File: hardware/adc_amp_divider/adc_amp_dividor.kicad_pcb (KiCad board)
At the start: 2 copper layers, 94 parts, among them M1 CONN_1, M2 CONN_1, P1 CONN_10X2, P2 CONN_4, P3 CONN_6, P4 CONN_3, U1 LMV324IDR, U2 LMV324IDR, U3 LMV324IDR

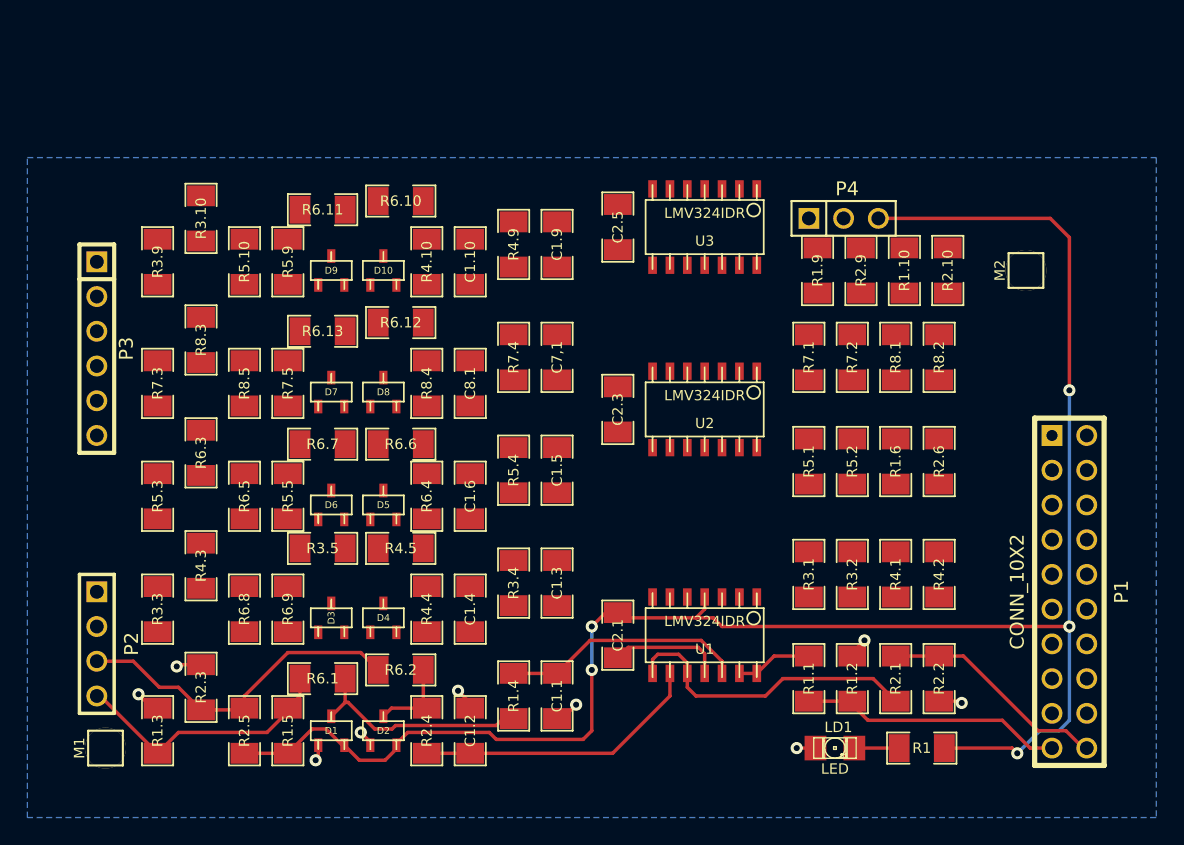
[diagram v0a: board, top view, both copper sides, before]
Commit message: 
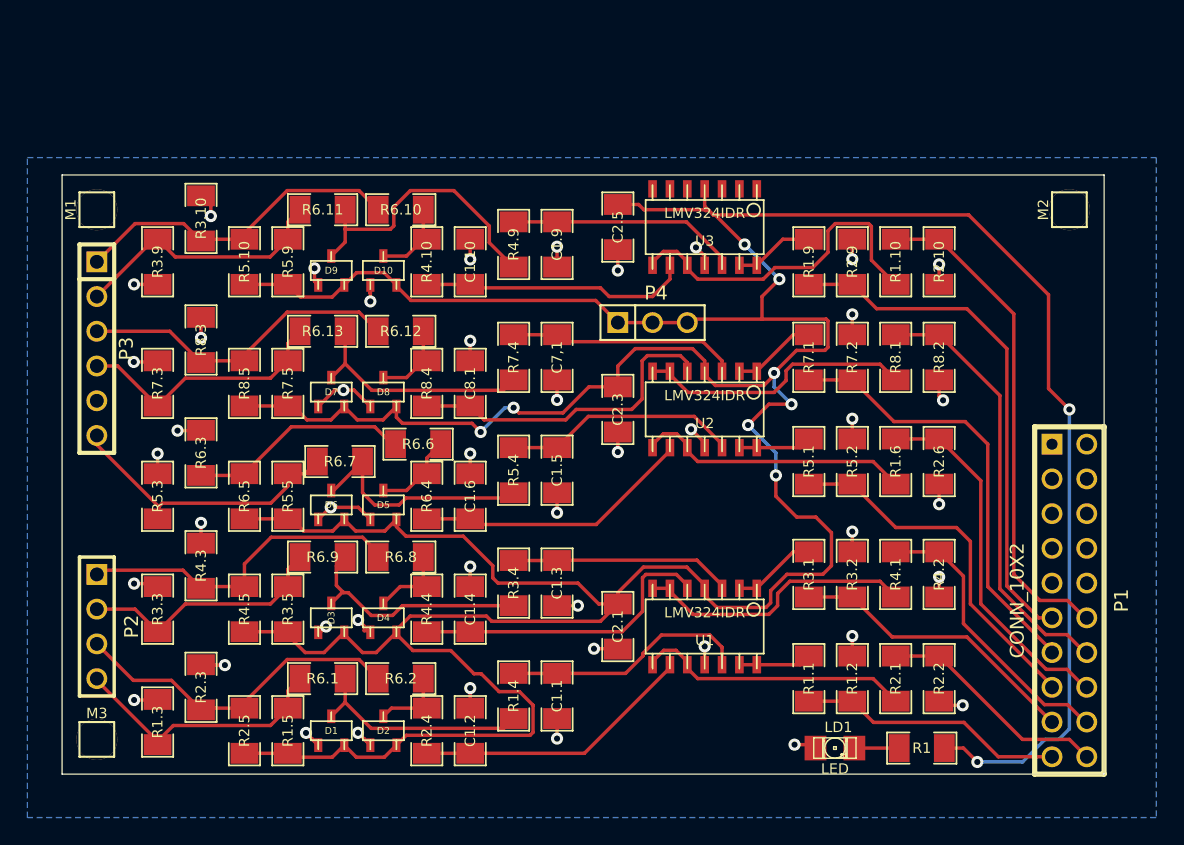
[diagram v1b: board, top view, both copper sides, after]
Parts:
- added M3: CONN_1, PIN_ARRAY_1, F.Cu at (92.7, 169.5)
- moved M1 39.4 mm to (92.7, 130.8)
- moved P4 15.9 mm to (133.3, 139.1)
- moved R4.5 12.3 mm to (103.5, 160.0), turned to 270 degrees
- moved R6.8 12.0 mm to (114.9, 156.2), turned to 0 degrees
- moved M2 5.46 mm to (163.8, 130.8)
- moved R3.5 5.12 mm to (106.7, 160.0), turned to 270 degrees
- moved R6.9 4.58 mm to (109.2, 156.2), turned to 0 degrees
- moved R6.7 1.80 mm to (110.5, 149.2)
- moved P2 1.27 mm to (92.7, 161.3)
- moved R6.6 1.27 mm to (116.2, 148.0)
- moved R1.10 0.90 mm to (151.1, 134.6)
- moved R1.9 0.90 mm to (144.8, 134.6)
- moved R2.10 0.90 mm to (154.3, 134.6)
- moved R2.9 0.90 mm to (148.0, 134.6)
- moved C2.1 0.64 mm to (130.8, 161.3)
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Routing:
- net VCC: track 134.0 -> 330.3 mm, vias 5 -> 10
- net GND: track 22.6 -> 76.8 mm, vias 9 -> 45
- net /OUT9: track 0.00 -> 38.0 mm
- net /OUT10: track 0.00 -> 36.6 mm
- net /OUT7: track 0.00 -> 32.2 mm
- net /OUT8: track 0.00 -> 31.9 mm
- net /OUT6: track 0.00 -> 26.8 mm
- net /OUT5: track 0.00 -> 26.7 mm
- net N-0000052: track 0.00 -> 25.4 mm
- net /INP10: track 0.00 -> 24.6 mm
- net /INP4: track 0.00 -> 24.5 mm
- net N-0000011: track 0.00 -> 23.9 mm
- net /INP8: track 0.00 -> 23.9 mm
- net N-0000065: track 0.00 -> 22.8 mm
- net /OUT3: track 0.00 -> 21.6 mm
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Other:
- board outline added: 76.2 x 43.8 mm
- net class Default: clearance 0.254 -> 0.2032
- rule trace_clearance: 0.254 -> 0.2032

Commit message: now 12 channels
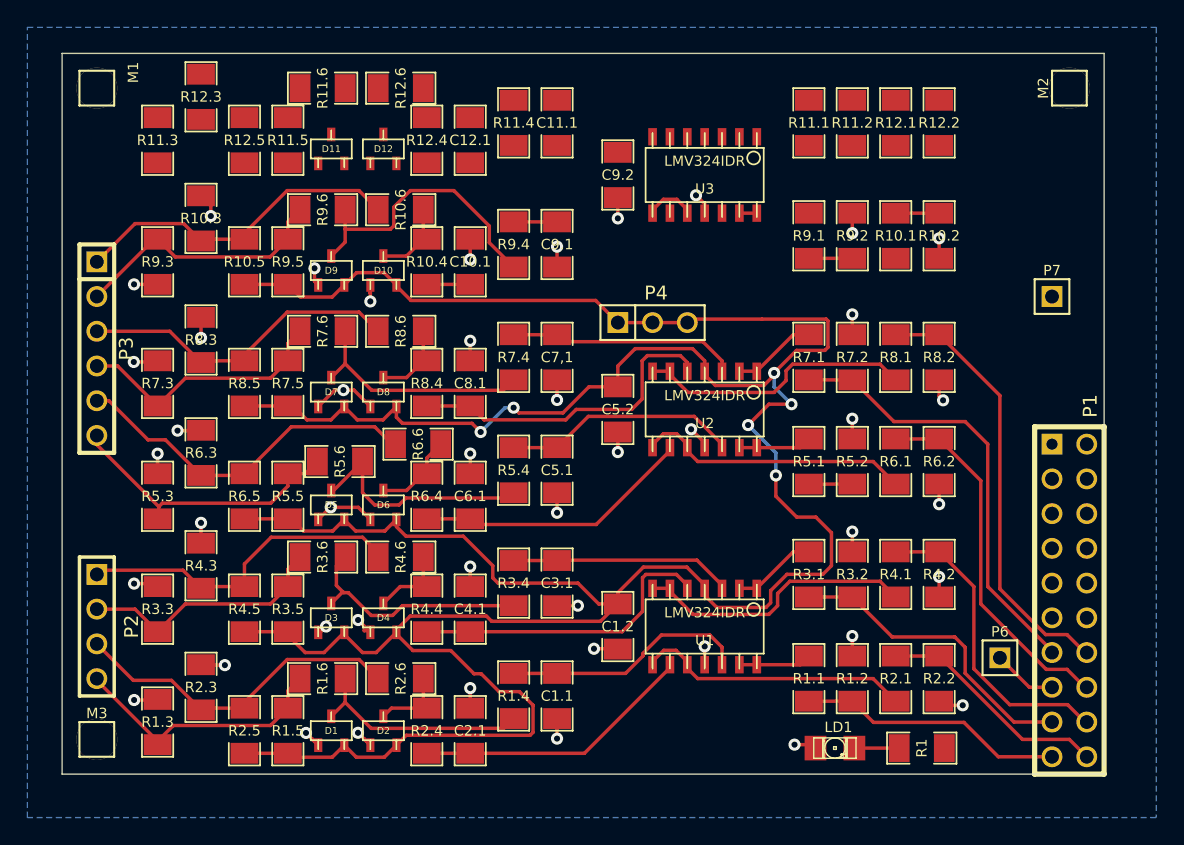
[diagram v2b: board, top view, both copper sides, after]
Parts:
- added C11.1: 0.01uF, SM1206, F.Cu at (126.4, 124.5)
- added C12.1: 0.01uF, SM1206, F.Cu at (120.0, 125.7)
- added D11: DOUBLE_SCHOTTKY, sot23, F.Cu at (109.9, 126.4)
- added D12: DOUBLE_SCHOTTKY, sot23, F.Cu at (113.7, 126.4)
- added P6: CONN_1, PIN_ARRAY_1, F.Cu at (158.8, 163.6)
- added P7: CONN_1, PIN_ARRAY_1, F.Cu at (162.6, 137.2)
- added R11.1: 1500, SM1206, F.Cu at (144.8, 124.5)
- added R11.2: 1500, SM1206, F.Cu at (148.0, 124.5)
- added R11.3: 500K, SM1206, F.Cu at (97.2, 125.7)
- added R11.4: 150, SM1206, F.Cu at (123.2, 124.5)
- added R11.5: 2700, SM1206, F.Cu at (106.7, 125.7)
- added R11.6: 10k, SM1206, F.Cu at (109.2, 121.9)
- added R12.1: 1500, SM1206, F.Cu at (151.1, 124.5)
- added R12.2: 1500, SM1206, F.Cu at (154.3, 124.5)
- added R12.3: 500K, SM1206, F.Cu at (100.3, 122.6)
- added R12.4: 150, SM1206, F.Cu at (116.8, 125.7)
- added R12.5: 2700, SM1206, F.Cu at (103.5, 125.7)
- added R12.6: 10k, SM1206, F.Cu at (114.9, 121.9)
- moved M1 8.89 mm to (92.7, 121.9)
- moved M2 8.89 mm to (163.8, 121.9)
- moved C9.2 3.81 mm to (130.8, 128.3)
- moved U3 3.81 mm to (137.2, 128.3)
- moved R10.1 1.91 mm to (151.1, 132.7)
- moved R10.2 1.91 mm to (154.3, 132.7)
- moved R9.1 1.91 mm to (144.8, 132.7)
- moved R9.2 1.91 mm to (148.0, 132.7)
- renumbered C2.1 to C1.2, C1.10 to C10.1, C1.2 to C2.1, C1.3 to C3.1, C1.4 to C4.1, C1.5 to C5.1, C2.3 to C5.2, C1.6 to C6.1, C1.9 to C9.1, C2.5 to C9.2, D6 to D5, D5 to D6, R6.1 to R1.6, R1.10 to R10.1, R2.10 to R10.2, R3.10 to R10.3, R4.10 to R10.4, R5.10 to R10.5, R6.10 to R10.6, R6.2 to R2.6, R6.9 to R3.6, R6.8 to R4.6, R6.7 to R5.6, R1.6 to R6.1, R2.6 to R6.2, R6.13 to R7.6, R6.12 to R8.6, R1.9 to R9.1, R2.9 to R9.2, R3.9 to R9.3, R4.9 to R9.4, R5.9 to R9.5, R6.11 to R9.6
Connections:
- P1 pad 10: (no net) -> /OUT11
- P1 pad 11: /OUT9 -> /OUT8
- P1 pad 12: /OUT10 -> /OUT9
- P1 pad 13: /OUT7 -> /OUT6
- P1 pad 14: /OUT8 -> /OUT7
- P1 pad 15: /OUT5 -> /PA5
- P1 pad 16: /OUT6 -> /OUT5
- P1 pad 7: (no net) -> /OUT12
- P1 pad 8: (no net) -> /PC0
- P1 pad 9: (no net) -> /OUT10
- P3 pad 5: (no net) -> /INP6
- R6.3 pad 1: N-0000079 (its old number) -> /INP6
- R6.5 pad 1: N-0000079 (its old number) -> /INP6
- R6.6 pad 1: N-0000079 (its old number) -> /INP6
- U3 pad 1: (no net) -> N-0000026
- U3 pad 2: (no net) -> N-0000026
- U3 pad 3: (no net) -> N-0000032
- U3 pad 5: (no net) -> N-0000035
- U3 pad 6: (no net) -> N-0000027
- U3 pad 7: (no net) -> N-0000027
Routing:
- net VCC: track 330.3 -> 241.2 mm, vias 10 -> 6
- net /OUT9: track 38.0 -> 3.18 mm
- net /OUT10: track 36.6 -> 3.18 mm
- net /INP6: track 0.00 -> 26.1 mm
- net /OUT8: track 31.9 -> 9.46 mm
- net N-0000012: track 25.4 -> 3.66 mm
- net N-000004: track 19.7 -> 3.17 mm
- net N-0000079 (its old number): track 16.2 -> 0.00 mm
- net N-000003: track 16.9 -> 3.17 mm
- net /OUT6: track 26.8 -> 32.2 mm
- net /PA5: track 0.00 -> 4.70 mm
- net N-0000011: track 5.87 -> 1.27 mm
- net /OUT5: track 26.7 -> 22.5 mm
- net /OUT7: track 32.2 -> 29.9 mm
- net /OUT4: track 21.2 -> 22.6 mm
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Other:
- board size 76.2 x 43.8 mm -> 76.2 x 52.7 mm

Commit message: my changes
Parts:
- added P8: CONN_2, PIN_ARRAY_2X1, F.Cu at (132.1, 121.9)
- P4: value CONN_3 -> CONN_2; footprint PIN_ARRAY_3X1 -> PIN_ARRAY_2X1
- moved P7 40.2 mm to (139.7, 170.2)
- moved P6 25.0 mm to (134.6, 170.2)
- moved P4 19.3 mm to (142.2, 121.9)
- moved C9.2 4.58 mm to (133.3, 132.1)
- moved U3 4.58 mm to (139.7, 132.1)
- moved R10.1 3.81 mm to (154.9, 132.7)
- moved R10.2 3.81 mm to (158.1, 132.7)
- moved R11.1 3.81 mm to (148.6, 124.5)
- moved R12.1 3.81 mm to (154.9, 124.5)
- moved R12.2 3.81 mm to (158.1, 124.5)
- moved R9.1 3.81 mm to (148.6, 132.7)
- moved R11.2 3.81 mm to (151.8, 124.5)
- moved R9.2 3.81 mm to (151.8, 132.7)
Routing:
- net /OUT6: track 32.2 -> 3.18 mm
- net VCC: track 241.2 -> 269.9 mm
- net /OUT7: track 29.9 -> 3.18 mm
- net /PA5: track 4.70 -> 28.3 mm
- net /OUT5: track 22.5 -> 3.18 mm
- net GND: track 76.8 -> 83.1 mm
- net /OUT8: track 9.46 -> 3.18 mm
- net N-000009: track 3.66 -> 0.00 mm

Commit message: fresh version
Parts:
- removed P8: CONN_2, PIN_ARRAY_2X1
- added P5: CONN_2, SIL-2, F.Cu at (134.6, 134.0)
- P2: value CONN_4 -> CONN_6; footprint PIN_ARRAY_4x1 -> PIN_ARRAY-6X1
- P4: value CONN_2 -> CONN_3; footprint PIN_ARRAY_2X1 -> PIN_ARRAY_3X1
- moved P7 36.6 mm to (162.6, 141.6)
- moved LD1 35.3 mm to (141.6, 135.3), turned to 270 degrees
- moved R1 33.6 mm to (140.3, 139.1), turned to 0 degrees
- moved P6 25.0 mm to (158.8, 163.6)
- moved P4 18.8 mm to (133.3, 138.4)
- moved P3 7.01 mm to (92.1, 134.0)
- moved C9.2 5.12 mm to (130.8, 127.6)
- moved U3 5.12 mm to (137.2, 127.6)
- moved P2 5.12 mm to (92.1, 156.2)
- moved R10.1 3.86 mm to (151.1, 132.1)
- moved R10.2 3.86 mm to (154.3, 132.1)
- moved R11.1 3.86 mm to (144.8, 123.8)
- moved R12.1 3.86 mm to (151.1, 123.8)
- moved R12.2 3.86 mm to (154.3, 123.8)
- moved R9.1 3.86 mm to (144.8, 132.1)
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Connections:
- P1 pad 2: (no net) -> GND
- P2 pad 1: /INP4 -> /INP6
- P2 pad 2: /INP3 -> /INP5
- P2 pad 3: /INP2 -> /INP4
- P2 pad 4: /INP1 -> /INP3
- P3 pad 1: /INP10 -> /INP12
- P3 pad 2: /INP9 -> /INP11
- P3 pad 3: /INP8 -> /INP10
- P3 pad 4: /INP7 -> /INP9
- P3 pad 5: /INP6 -> /INP8
- P3 pad 6: /INP5 -> /INP7
- R11.3 pad 1: /INP9 -> /INP11
- R11.5 pad 1: /INP9 -> /INP11
- R11.6 pad 1: /INP9 -> /INP11
- R12.3 pad 1: /INP10 -> /INP12
- R12.5 pad 1: /INP10 -> /INP12
- R12.6 pad 1: /INP10 -> /INP12
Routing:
- net /OUT11: track 0.00 -> 51.3 mm
- net /OUT12: track 0.00 -> 42.1 mm
- net /OUT9: track 3.17 -> 41.1 mm
- net /OUT7: track 3.18 -> 38.9 mm
- net /OUT10: track 3.18 -> 35.7 mm
- net /INP12: track 0.00 -> 28.9 mm
- net /OUT8: track 3.18 -> 29.0 mm
- net /OUT5: track 3.18 -> 28.9 mm
- net N-0000026: track 0.00 -> 24.4 mm
- net /INP11: track 0.00 -> 24.2 mm
- net /PA5: track 28.3 -> 4.70 mm
- net N-0000024: track 0.00 -> 21.8 mm
- net N-0000010: track 0.00 -> 21.1 mm
- net /OUT6: track 3.18 -> 22.4 mm
- net N-0000025: track 0.00 -> 18.5 mm
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- added copper zone on F.Cu, net GND
- added copper zone on F.Cu, net VCC
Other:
- outline, holes or cut-outs redrawn

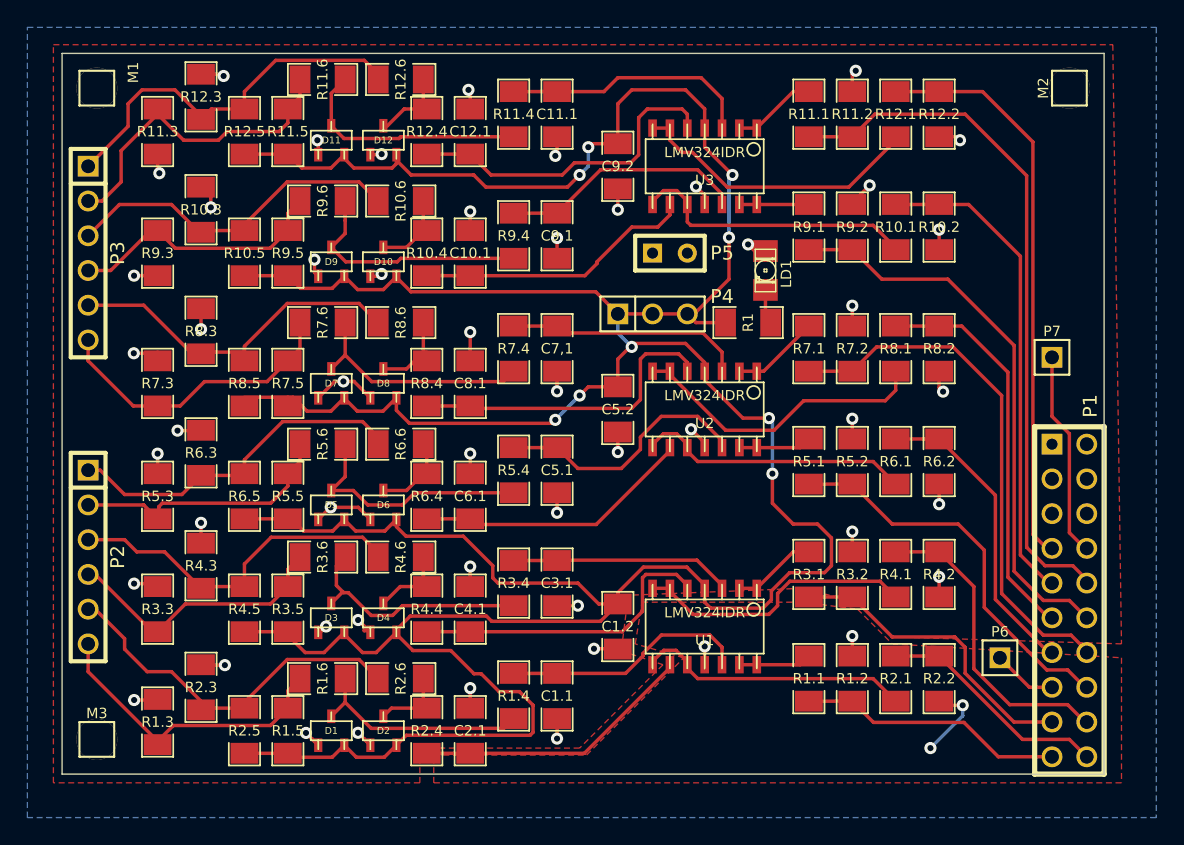
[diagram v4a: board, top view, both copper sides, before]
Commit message: 
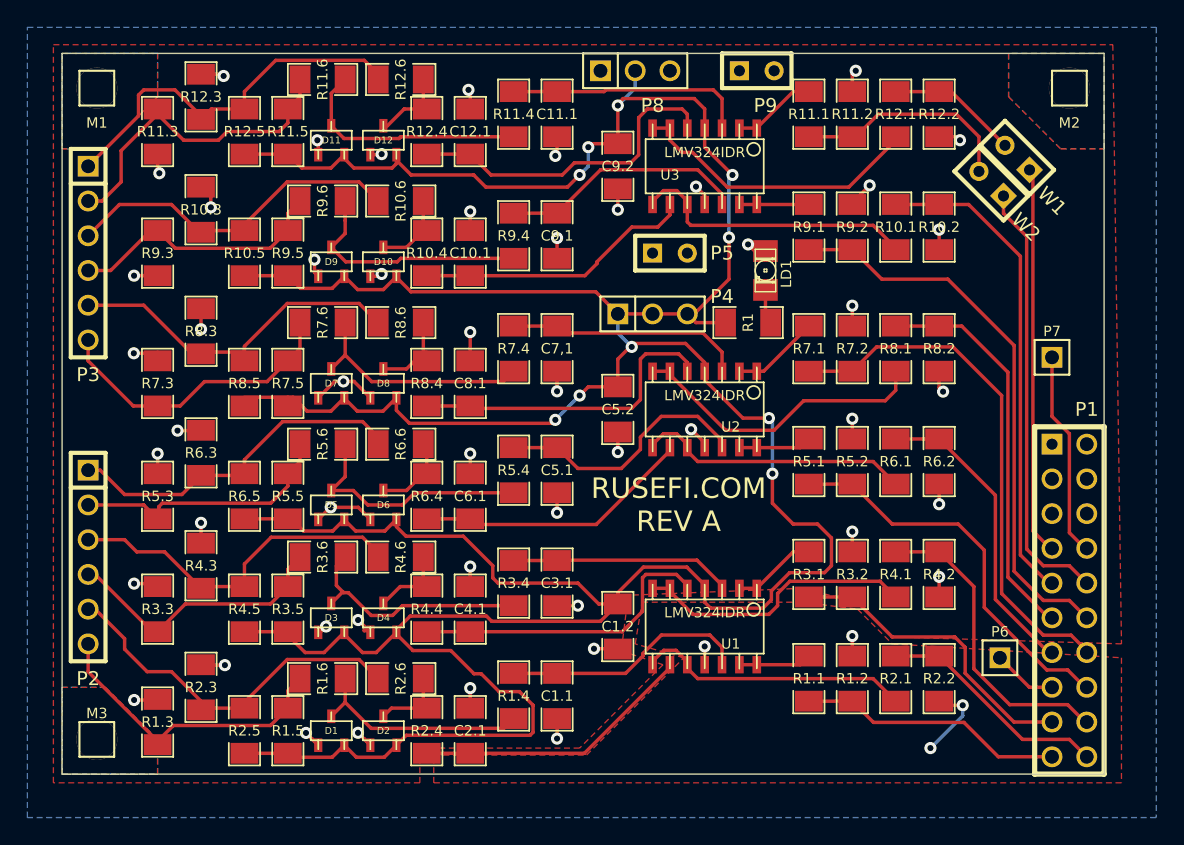
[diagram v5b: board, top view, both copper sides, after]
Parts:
- added P8: CONN_3, PIN_ARRAY_3X1, F.Cu at (132.1, 120.7)
- added P9: CONN_2, SIL-2, F.Cu at (141.0, 120.7)
- added W1: TEST, SIL-2, F.Cu at (160.0, 127.0)
- added W2: TEST, SIL-2, F.Cu at (158.1, 128.9)
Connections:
- R11.1 pad 2: /OUT11 -> N-0000035
- R11.2 pad 1: /OUT11 -> N-0000035
- R12.1 pad 2: /OUT12 -> N-0000034
- R12.2 pad 1: /OUT12 -> N-0000034
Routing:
- net /OUT11: track 51.3 -> 31.9 mm
- net N-0000035: track 0.00 -> 16.3 mm
- net /OUT12: track 42.1 -> 28.4 mm
- net N-0000034: track 0.00 -> 9.62 mm
- net VCC: track 284.8 -> 287.5 mm, vias 9 -> 10
- net N-0000030: track 18.5 -> 17.7 mm
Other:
- board text added: "RUSEFI.COM REV A"

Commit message: 150 > 100 on silkscreen
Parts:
- R1, R1.4, R10.4, R11.4, R12.4, R2.4, R3.4, R4.4, R5.4, R6.4, R7.4, R8.4, R9.4: value 150 -> 100
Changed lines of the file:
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@@
       (effects (font (size 0.762 0.762) (thickness 0.127)))
     )
-    (fp_text value 150 (at 0 0 90) (layer F.SilkS) hide
+    (fp_text value 100 (at 0 0 90) (layer F.SilkS) hide
       (effects (font (size 0.762 0.762) (thickness 0.127)))
     )
@@
       (effects (font (size 0.762 0.762) (thickness 0.127)))
     )
-    (fp_text value 150 (at 0 0 270) (layer F.SilkS) hide
+    (fp_text value 100 (at 0 0 270) (layer F.SilkS) hide
       (effects (font (size 0.762 0.762) (thickness 0.127)))
     )
@@
       (effects (font (size 0.762 0.762) (thickness 0.127)))
     )
-    (fp_text value 150 (at 0 0 90) (layer F.SilkS) hide
+    (fp_text value 100 (at 0 0 90) (layer F.SilkS) hide
       (effects (font (size 0.762 0.762) (thickness 0.127)))
     )
@@
       (effects (font (size 0.762 0.762) (thickness 0.127)))
     )
-    (fp_text value 150 (at 0 0 270) (layer F.SilkS) hide
+    (fp_text value 100 (at 0 0 270) (layer F.SilkS) hide
       (effects (font (size 0.762 0.762) (thickness 0.127)))
     )
@@
       (effects (font (size 0.762 0.762) (thickness 0.127)))
     )
-    (fp_text value 150 (at 0 0 270) (layer F.SilkS) hide
+    (fp_text value 100 (at 0 0 270) (layer F.SilkS) hide
       (effects (font (size 0.762 0.762) (thickness 0.127)))
     )
@@
       (effects (font (size 0.762 0.762) (thickness 0.127)))
     )
-    (fp_text value 150 (at 0 0 90) (layer F.SilkS) hide
+    (fp_text value 100 (at 0 0 90) (layer F.SilkS) hide
       (effects (font (size 0.762 0.762) (thickness 0.127)))
     )
@@
       (effects (font (size 0.762 0.762) (thickness 0.127)))
     )
-    (fp_text value 150 (at 0 0) (layer F.SilkS) hide
+    (fp_text value 100 (at 0 0) (layer F.SilkS) hide
       (effects (font (size 0.762 0.762) (thickness 0.127)))
     )
@@
       (effects (font (size 0.762 0.762) (thickness 0.127)))
     )
-    (fp_text value 150 (at 0 0 90) (layer F.SilkS) hide
+    (fp_text value 100 (at 0 0 90) (layer F.SilkS) hide
       (effects (font (size 0.762 0.762) (thickness 0.127)))
     )
@@
       (effects (font (size 0.762 0.762) (thickness 0.127)))
     )
-    (fp_text value 150 (at 0 0 270) (layer F.SilkS) hide
+    (fp_text value 100 (at 0 0 270) (layer F.SilkS) hide
       (effects (font (size 0.762 0.762) (thickness 0.127)))
     )
@@
       (effects (font (size 0.762 0.762) (thickness 0.127)))
     )
-    (fp_text value 150 (at 0 0 270) (layer F.SilkS) hide
+    (fp_text value 100 (at 0 0 270) (layer F.SilkS) hide
       (effects (font (size 0.762 0.762) (thickness 0.127)))
     )
@@
       (effects (font (size 0.762 0.762) (thickness 0.127)))
     )
-    (fp_text value 150 (at 0 0 90) (layer F.SilkS) hide
+    (fp_text value 100 (at 0 0 90) (layer F.SilkS) hide
       (effects (font (size 0.762 0.762) (thickness 0.127)))
     )
@@
       (effects (font (size 0.762 0.762) (thickness 0.127)))
     )
-    (fp_text value 150 (at 0 0 90) (layer F.SilkS) hide
+    (fp_text value 100 (at 0 0 90) (layer F.SilkS) hide
       (effects (font (size 0.762 0.762) (thickness 0.127)))
     )
@@
       (effects (font (size 0.762 0.762) (thickness 0.127)))
     )
-    (fp_text value 150 (at 0 0 270) (layer F.SilkS) hide
-      (effects (font (size 0.762 0.762) (thickness 0.127)))
-    )
+    (fp_text value 100 (at 0 0 270) (layer F.SilkS) hide
+      (effects (font (size 0.762 0.762) (thickness 0.127)))
+    )

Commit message: rev 0.2
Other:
- board text added: "RUSEFI.COM REV 0.2"
- board text removed: "RUSEFI.COM REV A"
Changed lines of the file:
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@@
     )
   )
-  (gr_text "RUSEFI.COM\nREV A" (at 135.255 152.4) (layer F.SilkS)
+  (gr_text "RUSEFI.COM\nREV 0.2" (at 135.255 152.4) (layer F.SilkS)
     (effects (font (size 1.5 1.5) (thickness 0.3)))
   )
